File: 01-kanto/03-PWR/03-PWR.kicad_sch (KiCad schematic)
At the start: 9 parts, among them Q1 PMOS, Q2 PMOS, Q3 PMOS, SW1 SW_SPST

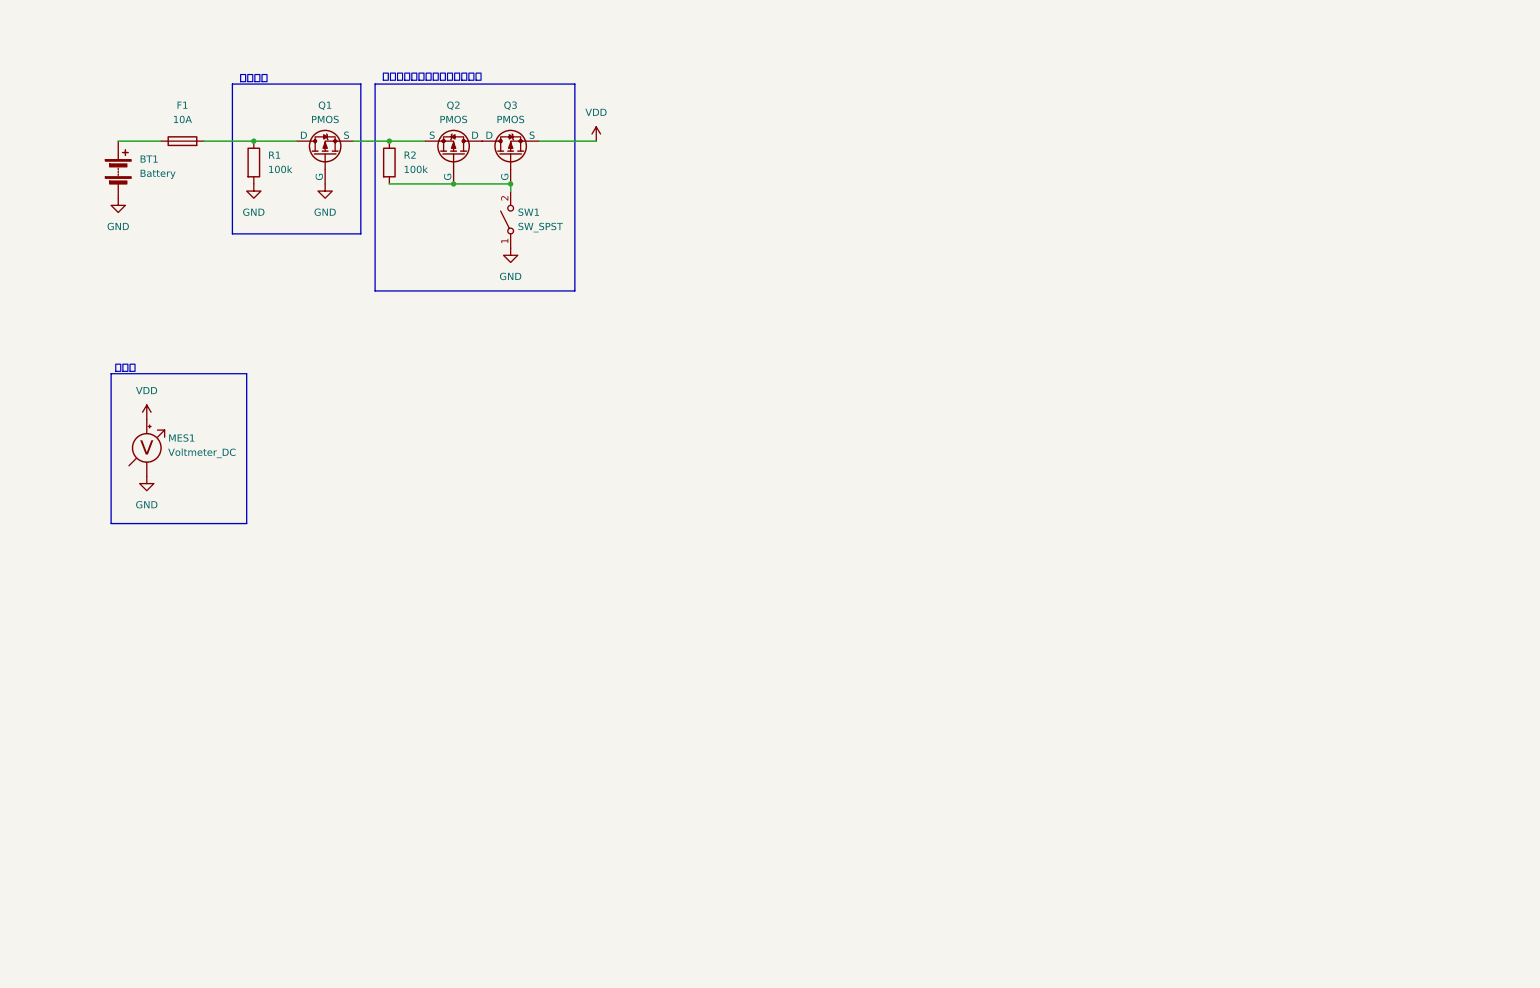
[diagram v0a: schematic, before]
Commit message: integrated ui with pwr
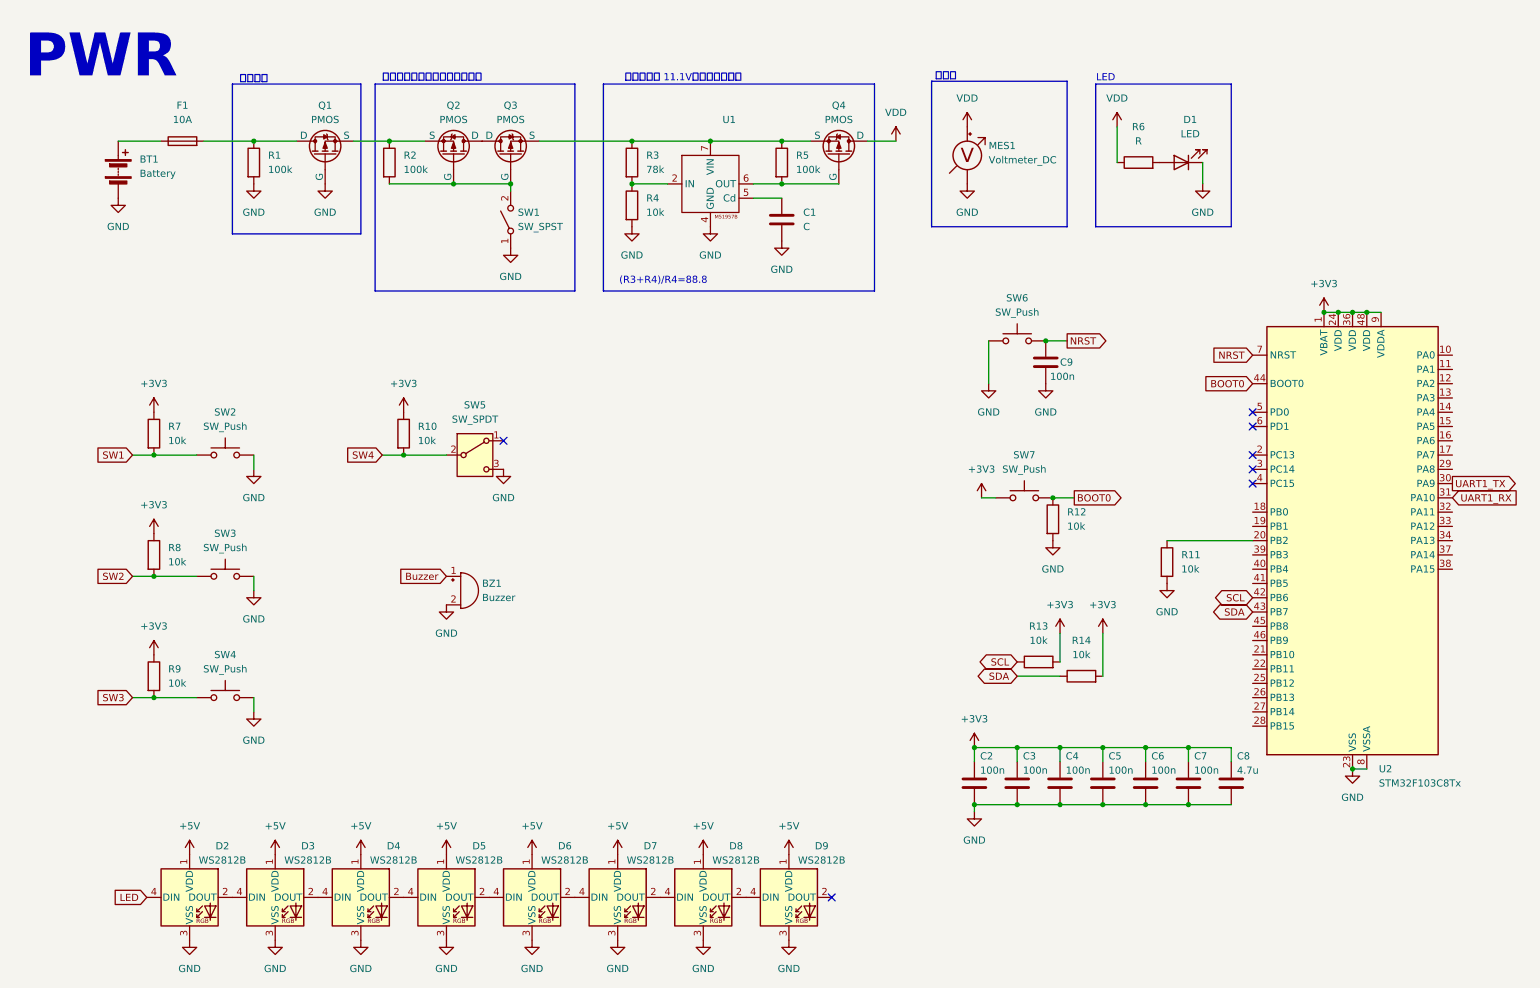
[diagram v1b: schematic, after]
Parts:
- added BZ1: Buzzer, symbol Device:Buzzer
- added C1: C, symbol Device:C
- added C2, C3, C4, C5, C6, C7, C9: 100n, symbol Device:C
- added C8: 4.7u, symbol Device:C
- added D1: LED, symbol Device:LED
- added D2, D3, D4, D5, D6, D7, D8, D9: WS2812B, LED_SMD:LED_WS2812B_PLCC4_5.0x5.0mm_P3.2mm, symbol LED:WS2812B
- added Q4: PMOS, symbol Simulation_SPICE:PMOS
- added R10, R11, R12, R13, R14, R4, R7, R8, R9: 10k, symbol Device:R
- added R3: 78k, symbol Device:R
- added R5: 100k, symbol Device:R
- added R6: R, symbol Device:R
- added SW2, SW3, SW4, SW6, SW7: SW_Push, symbol Switch:SW_Push
- added SW5: SW_SPDT, symbol Switch:SW_SPDT
- added U1: ~, symbol akizuki:M51957BFP
- added U2: STM32F103C8Tx, Package_QFP:LQFP-48_7x7mm_P0.5mm, symbol MCU_ST_STM32F1:STM32F103C8Tx
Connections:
- net GND: now also BZ1.2 (-), C1.2, C2.2, C3.2, C4.2, C5.2, C6.2, C7.2, C8.2, C9.2, D1.1 (K), D2.3 (VSS), D3.3 (VSS), D4.3 (VSS), D5.3 (VSS), D6.3 (VSS), D7.3 (VSS), D8.3 (VSS), D9.3 (VSS), R11.2, R12.2, R4.2, SW2.2, SW3.2, SW4.2, SW5.3 (C), SW6.1, U1.4 (GND), U2.23 (VSS), U2.35 (VSS), U2.47 (VSS), U2.8 (VSSA)
- net VDD: now also Q4.1 (D), R6.1; no longer Q3.3 (S)
- new net: Q3.3 (S), Q4.3 (S), R3.1, R5.1, U1.7 (VIN)
- new net: R3.2, R4.1, U1.2 (IN)
- new net: D1.2 (A), R6.2
- new net: Q4.2 (G), R5.2, U1.6 (OUT)
- new net: D6.2 (DOUT), D7.4 (DIN)
- new net: D5.2 (DOUT), D6.4 (DIN)
- new net: D4.2 (DOUT), D5.4 (DIN)
- new net: D3.2 (DOUT), D4.4 (DIN)
- new net: D2.2 (DOUT), D3.4 (DIN)
- new net: R11.1, U2.20 (PB2)
- new net: C1.1, U1.5 (Cd)
- new net: D8.2 (DOUT), D9.4 (DIN)
- new net: D7.2 (DOUT), D8.4 (DIN)
- new net +3V3: C2.1, C3.1, C4.1, C5.1, C6.1, C7.1, C8.1, R10.1, R13.2, R14.2, R7.1, R8.1, R9.1, SW7.1, U2.1 (VBAT), U2.24 (VDD), U2.36 (VDD), U2.48 (VDD), U2.9 (VDDA)
- new net +5V: D2.1 (VDD), D3.1 (VDD), D4.1 (VDD), D5.1 (VDD), D6.1 (VDD), D7.1 (VDD), D8.1 (VDD), D9.1 (VDD)
- new net BOOT0: R12.1, SW7.2, U2.44 (BOOT0)
- new net Buzzer: BZ1.1 (+)
- new net LED: D2.4 (DIN)
- new net NRST: C9.1, SW6.2, U2.7 (NRST)
- new net SCL: R13.1, U2.42 (PB6)
- new net SDA: R14.1, U2.43 (PB7)
- new net SW1: R7.2, SW2.1
- new net SW2: R8.2, SW3.1
- new net SW3: R9.2, SW4.1
- new net SW4: R10.2, SW5.2 (B)
- new net UART1_RX: U2.31 (PA10)
- new net UART1_TX: U2.30 (PA9)
- no-connect marks 0 -> 7
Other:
- note added: "(R3+R4)/R4=88.8"
- note added: "LED"
- note added: "PWR"
- note added: "低電圧防止 11.1V以下で強制遮断"
- title: 03-PWR -> 03-PWR&UI
- moved on the sheet: MES1
